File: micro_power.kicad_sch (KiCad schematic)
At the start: 24 parts, among them J7 4840.2201, J8 20021111-00010T4LF, J9 75869-105LF, Q1 BSS308PE, SW1 1825910-6, SW2 A11AH, U10 LM1086CS-5.0, U11 STM32G051K8T6, U9 LM1086CS-3.3, Y2 ABLS2-8.000MHZ-D4Y-T

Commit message: added connector footprints
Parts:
- J7: footprint (none) -> tbc:4840.2201
- SW2: footprint (none) -> tbc:A11AH
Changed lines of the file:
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@@
       (effects (font (size 1.27 1.27)))
     )
-    (property "Footprint" "" (at 73.66 140.97 0)
+    (property "Footprint" "tbc:A11AH" (at 73.66 140.97 0)
       (effects (font (size 1.27 1.27)) hide)
     )
@@
       (effects (font (size 1.27 1.27)))
     )
-    (property "Footprint" "" (at 57.15 143.51 0)
-      (effects (font (size 1.27 1.27)) hide)
-    )
+    (property "Footprint" "tbc:4840.2201" (at 57.15 143.51 0)
+      (effects (font (size 1.27 1.27)) hide)
+    )

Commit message: mosfet and tantalum footprints
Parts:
- C51: footprint (none) -> tbc:293D_C
- C54, C55: footprint (none) -> tbc:593D_D
- Q1: footprint (none) -> tbc:SOT23
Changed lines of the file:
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@@
       (effects (font (size 1.27 1.27)) (justify left))
     )
-    (property "Footprint" "" (at 139.7 168.91 0)
+    (property "Footprint" "tbc:593D_D" (at 139.7 168.91 0)
       (effects (font (size 1.27 1.27)) hide)
     )
@@
       (effects (font (size 1.27 1.27)))
     )
-    (property "Footprint" "" (at 88.9 142.24 0)
+    (property "Footprint" "tbc:SOT23" (at 88.9 142.24 0)
       (effects (font (size 1.27 1.27)) hide)
     )
@@
       (effects (font (size 1.27 1.27)) (justify left))
     )
-    (property "Footprint" "" (at 139.7 146.05 0)
+    (property "Footprint" "tbc:593D_D" (at 139.7 146.05 0)
       (effects (font (size 1.27 1.27)) hide)
     )
@@
       (effects (font (size 1.27 1.27)) (justify left))
     )
-    (property "Footprint" "" (at 91.44 151.13 0)
-      (effects (font (size 1.27 1.27)) hide)
-    )
+    (property "Footprint" "tbc:293D_C" (at 91.44 151.13 0)
+      (effects (font (size 1.27 1.27)) hide)
+    )

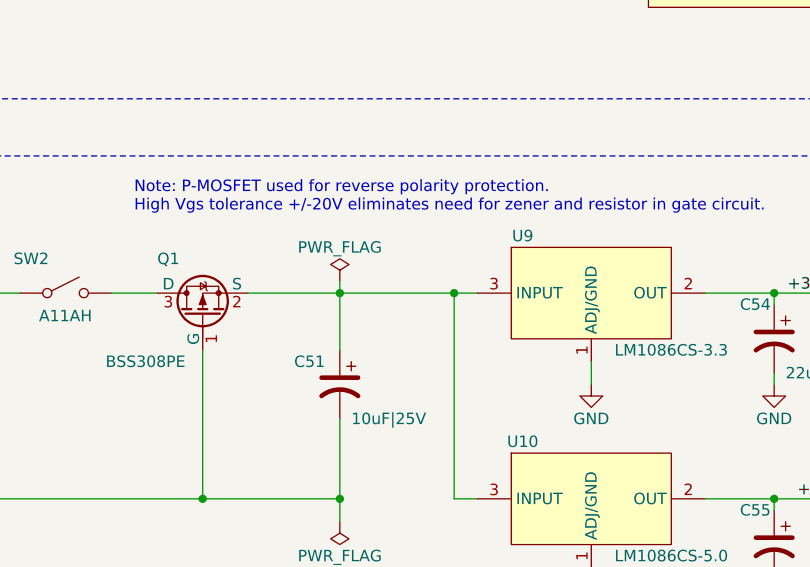
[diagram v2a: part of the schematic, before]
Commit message: completed power footprints
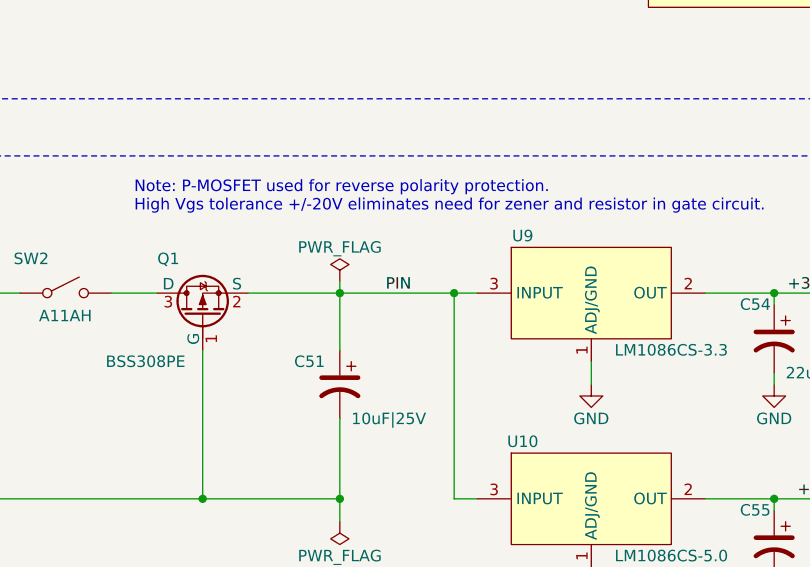
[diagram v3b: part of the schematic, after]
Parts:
- U10, U9: footprint (none) -> tbc:TO-263_4.83mm
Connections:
- net PIN: now reaches C51.1, Q1.2 (S), U10.3 (INPUT), U9.3 (INPUT)
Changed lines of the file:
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@@
     (effects (font (size 1.27 1.27)) (justify right bottom))
+  )
+  (label "PIN" (at 109.22 140.97 0) (fields_autoplaced)
+    (effects (font (size 1.27 1.27)) (justify left bottom))
   )
   (label "SCL2" (at 209.55 50.8 0) (fields_autoplaced)
@@
       (effects (font (size 1.27 1.27)))
     )
-    (property "Footprint" "" (at 120.65 170.18 0)
+    (property "Footprint" "tbc:TO-263_4.83mm" (at 120.65 170.18 0)
       (effects (font (size 1.27 1.27)) hide)
     )
@@
       (effects (font (size 1.27 1.27)))
     )
-    (property "Footprint" "" (at 120.65 147.32 0)
-      (effects (font (size 1.27 1.27)) hide)
-    )
+    (property "Footprint" "tbc:TO-263_4.83mm" (at 120.65 147.32 0)
+      (effects (font (size 1.27 1.27)) hide)
+    )

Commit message: footprints and 3d models for caps, connectors
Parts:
- added MH1, MH2, MH3, MH4: MH_7.4MMNCx3.2MMD, tbc:MH_7.4MMCx3.2MMD_NON_COPPER_NPTH, symbol tbc:MH_7.4MMNCx3.2MMD
- C50, C52, C53, C56, C57: footprint (none) -> tbc:C0603
- J8: footprint (none) -> tbc:20021111-00010T4LF
- SW1: footprint (none) -> tbc:1825910-6
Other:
- note added: "Mounting Holes"
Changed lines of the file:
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@@
+    (fill (type none))
+  )
+  (rectangle (start 176.53 135.89) (end 209.55 158.75)
+    (stroke (width 0) (type dash))
     (fill (type none))
   )
@@
     (effects (font (size 1.27 1.27)) (justify right bottom))
   )
+  (text "Mounting Holes" (at 177.8 139.7 0)
+    (effects (font (size 2.54 2.54)) (justify left bottom))
+  )
   (text "Microcontroller" (at 39.37 27.94 0)
     (effects (font (size 2.54 2.54)) (justify left bottom))
@@
     )
   )
+  (symbol (lib_id "tbc:MH_7.4MMNCx3.2MMD") (at 187.96 154.94 0) (unit 1)
+    (in_bom yes) (on_board yes) (dnp no)
+    (property "Reference" "MH2" (at 186.69 151.13 0)
+      (effects (font (size 1.27 1.27)) (justify left))
+    )
+    (property "Value" "MH_7.4MMNCx3.2MMD" (at 189.23 158.75 0)
+      (effects (font (size 1.27 1.27)) hide)
+    )
+    (property "Footprint" "tbc:MH_7.4MMCx3.2MMD_NON_COPPER_NPTH" (at 187.96 161.29 0) (show_name)
+      (effects (font (size 1.27 1.27)) hide)
+    )
+    (property "Datasheet" "" (at 187.96 152.4 0)
+      (effects (font (size 1.27 1.27)) hide)
+    )
+    (property "Sim.Enable" "0" (at 187.96 158.75 0)
+      (effects (font (size 1.27 1.27)) hide)
+    )
+    (instances
+      (project "tbc"
+        (path "/9df71e53-7941-4fd3-a17d-93619e4e3e02/5f11175b-e91a-4557-963e-2b2820dad3c4"
+          (reference "MH2") (unit 1)
+        )
+      )
+    )
+  )
   (symbol (lib_id "tbc:593D226X9025D2TE3") (at 152.4 168.91 270) (unit 1)
     (in_bom yes) (on_board yes) (dnp no)
@@
       (effects (font (size 1.27 1.27)))
     )
-    (property "Footprint" "" (at 59.69 82.55 0)
+    (property "Footprint" "tbc:1825910-6" (at 59.69 82.55 0)
       (effects (font (size 1.27 1.27)) hide)
     )
@@
       (effects (font (size 1.27 1.27)))
     )
-    (property "Footprint" "" (at 166.37 54.61 0)
+    (property "Footprint" "tbc:C0603" (at 166.37 54.61 0)
       (effects (font (size 1.27 1.27)) hide)
     )
@@
       (effects (font (size 1.27 1.27)))
     )
-    (property "Footprint" "" (at 166.37 44.45 0)
+    (property "Footprint" "tbc:C0603" (at 166.37 44.45 0)
       (effects (font (size 1.27 1.27)) hide)
     )
@@
       (effects (font (size 1.27 1.27)))
     )
-    (property "Footprint" "" (at 144.78 34.29 0)
+    (property "Footprint" "tbc:C0603" (at 144.78 34.29 0)
       (effects (font (size 1.27 1.27)) hide)
     )
@@
         (path "/9df71e53-7941-4fd3-a17d-93619e4e3e02/5f11175b-e91a-4557-963e-2b2820dad3c4"
           (reference "#PWR059") (unit 1)
+        )
+      )
+    )
+  )
+  (symbol (lib_id "tbc:MH_7.4MMNCx3.2MMD") (at 196.85 146.05 0) (unit 1)
+    (in_bom yes) (on_board yes) (dnp no)
+    (property "Reference" "MH3" (at 195.58 142.24 0)
+      (effects (font (size 1.27 1.27)) (justify left))
+    )
+    (property "Value" "MH_7.4MMNCx3.2MMD" (at 198.12 149.86 0)
+      (effects (font (size 1.27 1.27)) hide)
+    )
+    (property "Footprint" "tbc:MH_7.4MMCx3.2MMD_NON_COPPER_NPTH" (at 196.85 152.4 0) (show_name)
+      (effects (font (size 1.27 1.27)) hide)
+    )
+    (property "Datasheet" "" (at 196.85 143.51 0)
+      (effects (font (size 1.27 1.27)) hide)
+    )
+    (property "Sim.Enable" "0" (at 196.85 149.86 0)
+      (effects (font (size 1.27 1.27)) hide)
+    )
+    (instances
+      (project "tbc"
+        (path "/9df71e53-7941-4fd3-a17d-93619e4e3e02/5f11175b-e91a-4557-963e-2b2820dad3c4"
+          (reference "MH3") (unit 1)
         )
       )
@@
     )
   )
+  (symbol (lib_id "tbc:MH_7.4MMNCx3.2MMD") (at 187.96 146.05 0) (unit 1)
+    (in_bom yes) (on_board yes) (dnp no)
+    (property "Reference" "MH1" (at 186.69 142.24 0)
+      (effects (font (size 1.27 1.27)) (justify left))
+    )
+    (property "Value" "MH_7.4MMNCx3.2MMD" (at 189.23 149.86 0)
+      (effects (font (size 1.27 1.27)) hide)
+    )
+    (property "Footprint" "tbc:MH_7.4MMCx3.2MMD_NON_COPPER_NPTH" (at 187.96 152.4 0) (show_name)
+      (effects (font (size 1.27 1.27)) hide)
+    )
+    (property "Datasheet" "" (at 187.96 143.51 0)
+      (effects (font (size 1.27 1.27)) hide)
+    )
+    (property "Sim.Enable" "0" (at 187.96 149.86 0)
+      (effects (font (size 1.27 1.27)) hide)
+    )
+    (instances
+      (project "tbc"
+        (path "/9df71e53-7941-4fd3-a17d-93619e4e3e02/5f11175b-e91a-4557-963e-2b2820dad3c4"
+          (reference "MH1") (unit 1)
+        )
+      )
+    )
+  )
   (symbol (lib_id "tbc:LM1086CS-3.3") (at 132.08 140.97 0) (unit 1)
     (in_bom yes) (on_board yes) (dnp no)
@@
       (effects (font (size 1.27 1.27)))
     )
-    (property "Footprint" "" (at 96.52 72.39 0)
+    (property "Footprint" "tbc:20021111-00010T4LF" (at 96.52 72.39 0)
       (effects (font (size 1.27 1.27)) hide)
     )
@@
       (effects (font (size 1.27 1.27)))
     )
-    (property "Footprint" "" (at 59.69 96.52 0)
+    (property "Footprint" "tbc:C0603" (at 59.69 96.52 0)
       (effects (font (size 1.27 1.27)) hide)
     )
@@
     )
     (property "Footprint" "tbc:R0603" (at 76.2 55.88 0) (show_name)
-      (effects (font (size 1.27 1.27)))
+      (effects (font (size 1.27 1.27)) hide)
     )
     (property "Datasheet" "https://www.mouser.com/datasheet/2/447/YAGEO_PYu_RC_Group_51_RoHS_L_12-3313492.pdf" (at 81.28 72.39 0) (show_name)
@@
     )
   )
+  (symbol (lib_id "tbc:MH_7.4MMNCx3.2MMD") (at 196.85 154.94 0) (unit 1)
+    (in_bom yes) (on_board yes) (dnp no)
+    (property "Reference" "MH4" (at 195.58 151.13 0)
+      (effects (font (size 1.27 1.27)) (justify left))
+    )
+    (property "Value" "MH_7.4MMNCx3.2MMD" (at 198.12 158.75 0)
+      (effects (font (size 1.27 1.27)) hide)
+    )
+    (property "Footprint" "tbc:MH_7.4MMCx3.2MMD_NON_COPPER_NPTH" (at 196.85 161.29 0) (show_name)
+      (effects (font (size 1.27 1.27)) hide)
+    )
+    (property "Datasheet" "" (at 196.85 152.4 0)
+      (effects (font (size 1.27 1.27)) hide)
+    )
+    (property "Sim.Enable" "0" (at 196.85 158.75 0)
+      (effects (font (size 1.27 1.27)) hide)
+    )
+    (instances
+      (project "tbc"
+        (path "/9df71e53-7941-4fd3-a17d-93619e4e3e02/5f11175b-e91a-4557-963e-2b2820dad3c4"
+          (reference "MH4") (unit 1)
+        )
+      )
+    )
+  )
   (symbol (lib_id "tbc:+3V3") (at 85.09 46.99 0) (unit 1)
     (in_bom yes) (on_board yes) (dnp no)
@@
       (effects (font (size 1.27 1.27)))
     )
-    (property "Footprint" "" (at 132.08 34.29 0)
-      (effects (font (size 1.27 1.27)) hide)
-    )
+    (property "Footprint" "tbc:C0603" (at 132.08 34.29 0)
+      (effects (font (size 1.27 1.27)) hide)
+    )

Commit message: added connector and diode footprint, more layout
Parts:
- J9: footprint (none) -> tbc:75869-105LF
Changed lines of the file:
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@@
       (effects (font (size 1.27 1.27)) (justify left))
     )
-    (property "Footprint" "" (at 217.17 35.56 0)
+    (property "Footprint" "tbc:75869-105LF" (at 217.17 35.56 0)
       (effects (font (size 1.27 1.27)) hide)
     )

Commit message: added footprints for crystals and updated layout
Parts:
- Y2: footprint (none) -> tbc:ABLS2
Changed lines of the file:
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@@
       (effects (font (size 0.635 0.635)))
     )
-    (property "Footprint" "" (at 127 55.88 0)
+    (property "Footprint" "tbc:ABLS2" (at 127 55.88 0)
       (effects (font (size 1.27 1.27)) hide)
     )

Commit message: add PEC11R footprint, minor enhancements to layout
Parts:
- MH1, MH2, MH3, MH4: now left out of the parts list
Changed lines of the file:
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@@
   )
   (symbol (lib_id "tbc:MH_7.4MMNCx3.2MMD") (at 187.96 154.94 0) (unit 1)
-    (in_bom yes) (on_board yes) (dnp no)
+    (in_bom no) (on_board yes) (dnp no)
     (property "Reference" "MH2" (at 186.69 151.13 0)
       (effects (font (size 1.27 1.27)) (justify left))
@@
   )
   (symbol (lib_id "tbc:MH_7.4MMNCx3.2MMD") (at 196.85 146.05 0) (unit 1)
-    (in_bom yes) (on_board yes) (dnp no)
+    (in_bom no) (on_board yes) (dnp no)
     (property "Reference" "MH3" (at 195.58 142.24 0)
       (effects (font (size 1.27 1.27)) (justify left))
@@
   )
   (symbol (lib_id "tbc:MH_7.4MMNCx3.2MMD") (at 187.96 146.05 0) (unit 1)
-    (in_bom yes) (on_board yes) (dnp no)
+    (in_bom no) (on_board yes) (dnp no)
     (property "Reference" "MH1" (at 186.69 142.24 0)
       (effects (font (size 1.27 1.27)) (justify left))
@@
   )
   (symbol (lib_id "tbc:MH_7.4MMNCx3.2MMD") (at 196.85 154.94 0) (unit 1)
-    (in_bom yes) (on_board yes) (dnp no)
+    (in_bom no) (on_board yes) (dnp no)
     (property "Reference" "MH4" (at 195.58 151.13 0)
       (effects (font (size 1.27 1.27)) (justify left))
